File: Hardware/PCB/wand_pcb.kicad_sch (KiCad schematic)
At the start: 20 parts, among them SW1 SW_Push, U1 ESP32-MINI-1, U4 ICM-20948, U5 MIC5504-1.8YM5-TR, U6 TCA9416DDFR

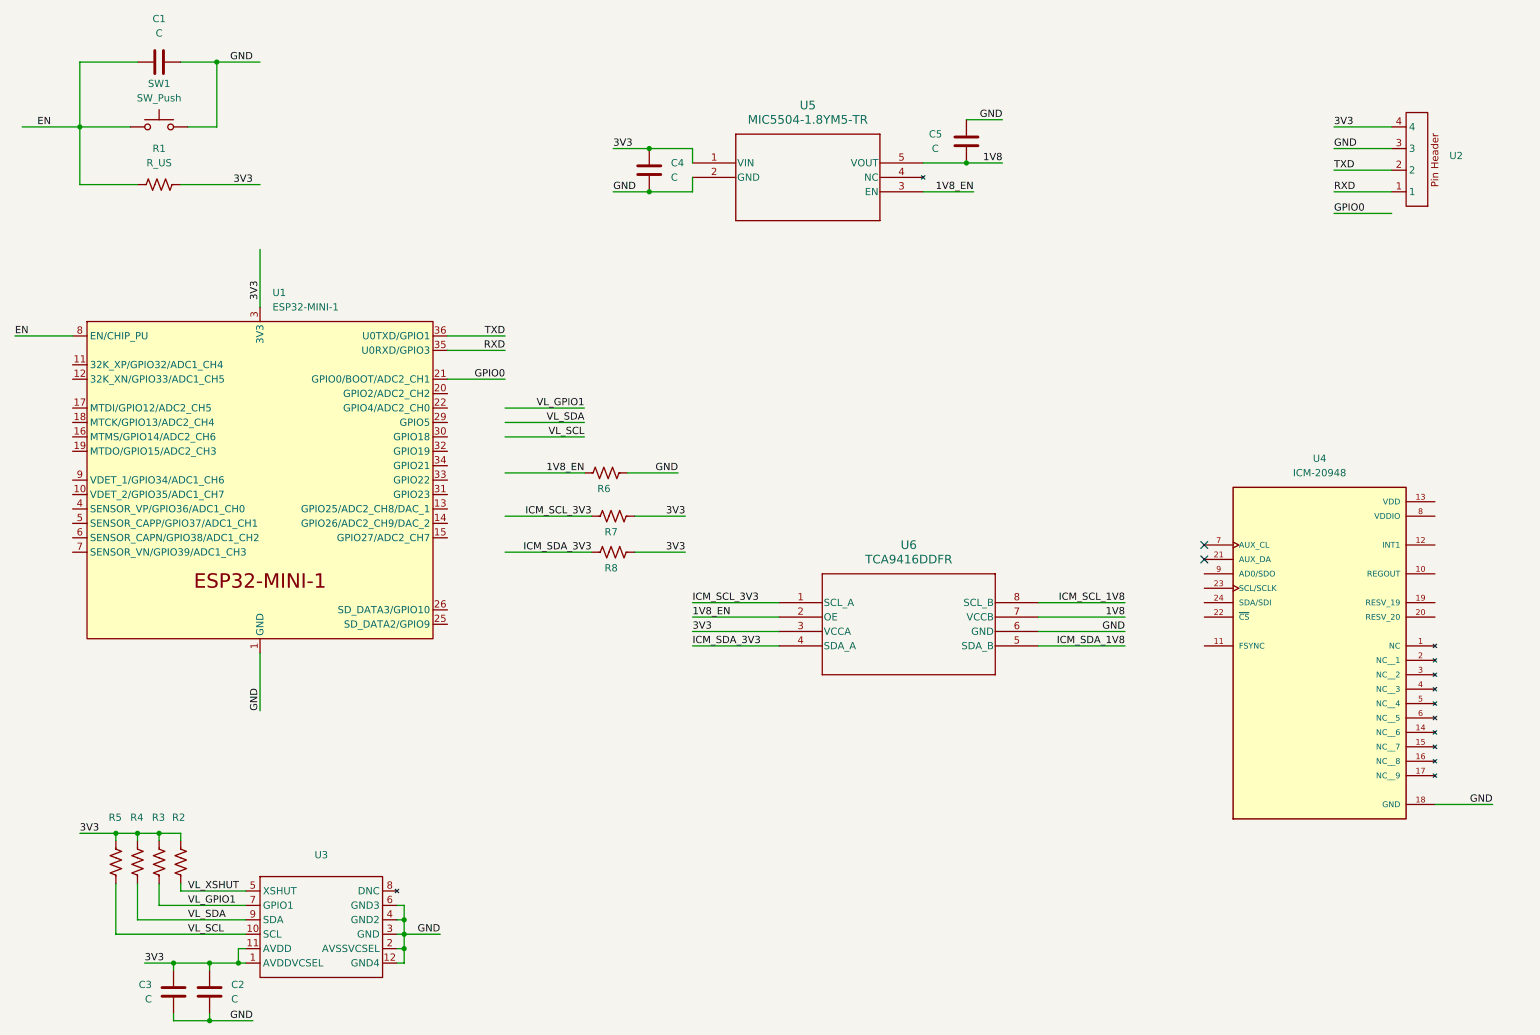
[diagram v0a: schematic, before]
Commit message: working on power supply conversion
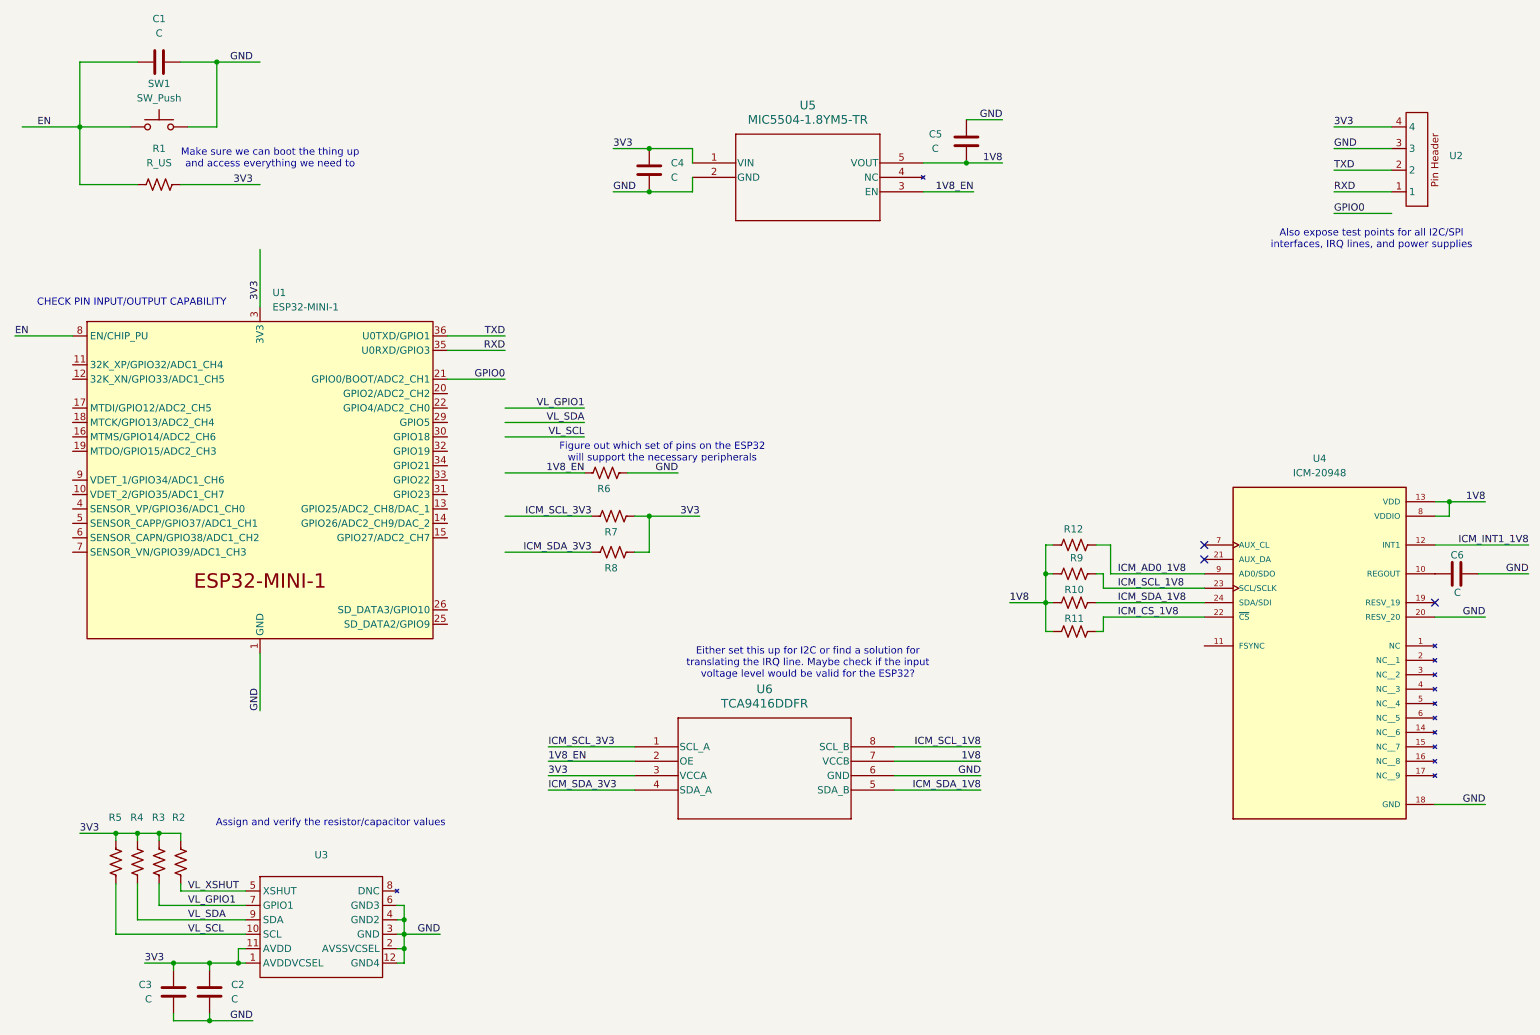
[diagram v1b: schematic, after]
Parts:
- added C6: C, Capacitor_SMD:C_1206_3216Metric_Pad1.33x1.80mm_HandSolder, symbol Device:C
- added R10, R11, R12, R9: R_US, Resistor_SMD:R_1206_3216Metric_Pad1.30x1.75mm_HandSolder, symbol Device:R_US
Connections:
- net 1V8: now also U4.13 (VDD), U4.8 (VDDIO), R10.2, R11.2, R12.1, R9.1
- net GND: now also U4.20 (RESV_20), C6.1
- net ICM_SCL_1V8: now also U4.23 (SCL/SCLK), R9.2
- net ICM_SDA_1V8: now also U4.24 (SDA/SDI), R10.1
- net at U4.10 (REGOUT): now also C6.2
- net ICM_INT1_1V8: now reaches U4.12 (INT1)
- net ICM_CS_1V8: now reaches U4.22 (~{CS})
- net ICM_CS_1V8: now also R11.1
- net ICM_AD0_1V8: now reaches U4.9 (AD0/SDO)
- net ICM_AD0_1V8: now also R12.2
- no-connect marks 2 -> 3
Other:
- note added: "Also expose test points for all I2C/SPI interfaces, IRQ lines, and power supplies"
- note added: "Assign and verify the resistor/capacitor values"
- note added: "CHECK PIN INPUT/OUTPUT CAPABILITY"
- note added: "Either set this up for I2C or find a solution for translating the IRQ line. Maybe check if the input voltage level would be valid for the ESP32?"
- note added: "Figure out which set of pins on the ESP32 will support the necessary peripherals"
- note added: "Make sure we can boot the thing up and access everything we need to"
- moved on the sheet: U6

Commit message: Added accel, gyro, mag
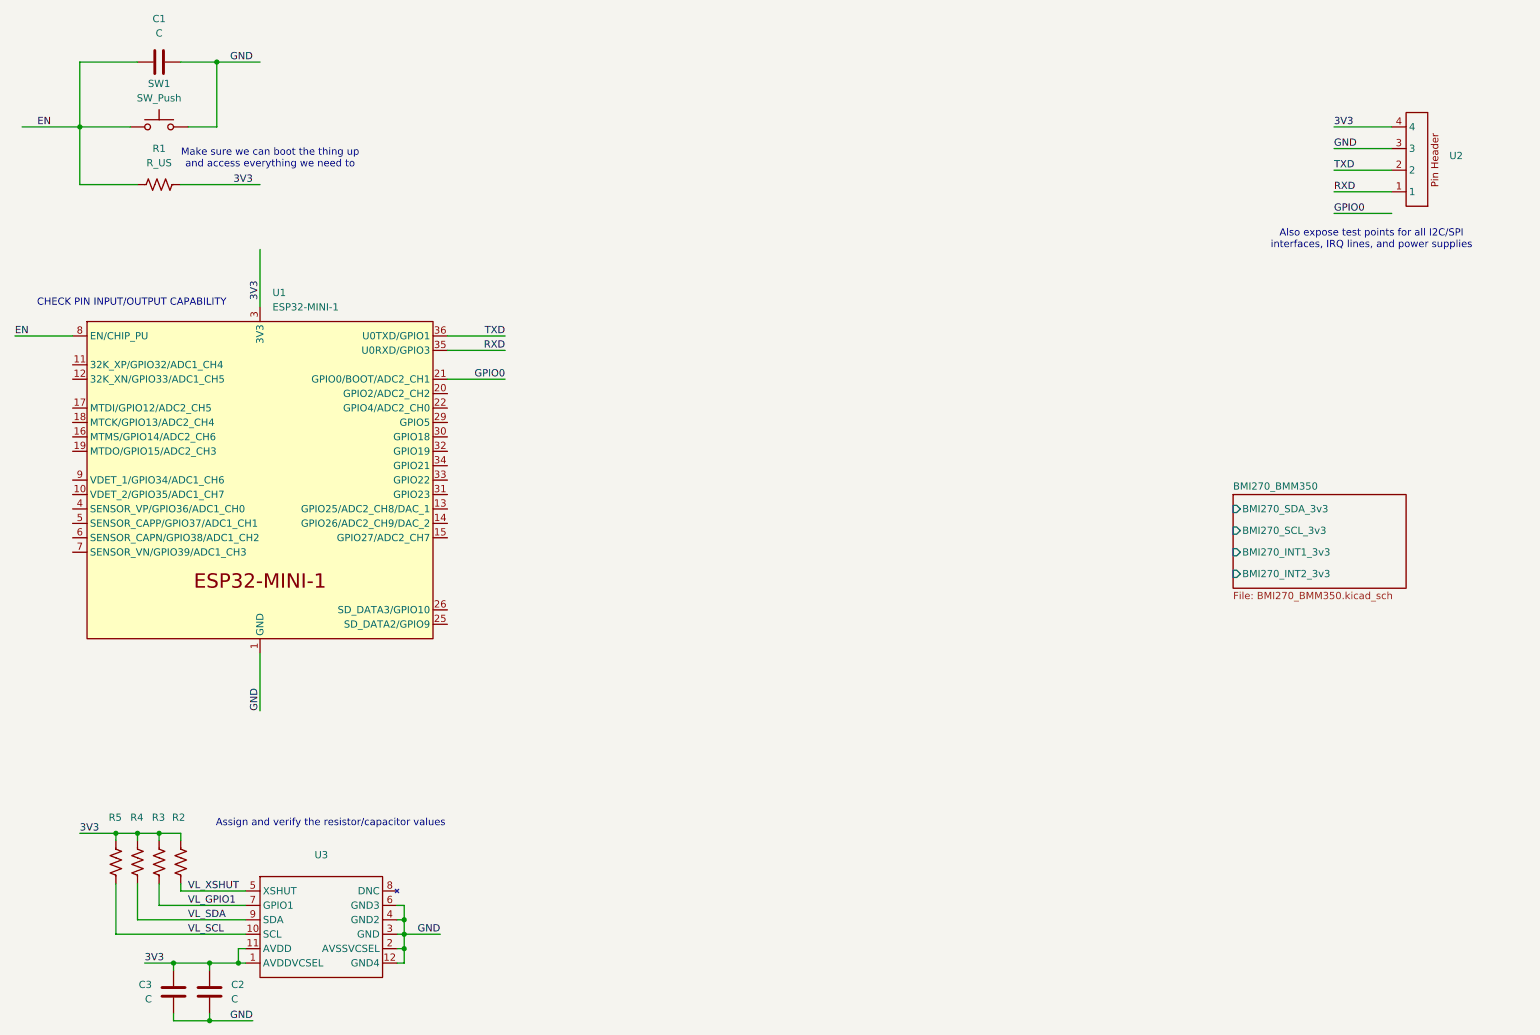
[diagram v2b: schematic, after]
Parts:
- removed C4, C5, C6: C, Capacitor_SMD:C_1206_3216Metric_Pad1.33x1.80mm_HandSolder, symbol Device:C
- removed R10, R11, R12, R6, R7, R8, R9: R_US, Resistor_SMD:R_1206_3216Metric_Pad1.30x1.75mm_HandSolder, symbol Device:R_US
- removed U4: ICM-20948, ICM-20948:QFN40P300X300X105-24N, symbol ICM-20948:ICM-20948
- removed U5: MIC5504-1.8YM5-TR, SOT23-5LD-PL-1_MCH, symbol MIC5504-1.8YM5:MIC5504-1.8YM5-TR
- removed U6: TCA9416DDFR, SOT_16DDFR_TEX, symbol TCA9416DDFR:TCA9416DDFR
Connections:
- no-connect marks 3 -> 0
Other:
- added sheet BMI270_BMM350 (BMI270_BMM350.kicad_sch)
- note removed: "Either set this up for I2C or find a solution for translating the IRQ line. Maybe check if the input voltage level would be valid for the ESP32?"
- note removed: "Figure out which set of pins on the ESP32 will support the necessary peripherals"
